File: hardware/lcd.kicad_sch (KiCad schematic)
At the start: 7 parts, among them J3 Conn_01x40, Q3 AO3400A

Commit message: add (analog) mems microphone
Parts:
- R29, R30, R31: footprint (none) -> Resistor_SMD:R_0603_1608Metric
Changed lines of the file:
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@@
 			)
 		)
-		(property "Footprint" ""
+		(property "Footprint" "Resistor_SMD:R_0603_1608Metric"
 			(at 83.82 173.482 90)
 			(effects
@@
 			)
 		)
-		(property "Footprint" ""
+		(property "Footprint" "Resistor_SMD:R_0603_1608Metric"
 			(at 46.99 109.728 90)
 			(effects
@@
 			)
 		)
-		(property "Footprint" ""
+		(property "Footprint" "Resistor_SMD:R_0603_1608Metric"
 			(at 83.82 183.642 90)
 			(effects

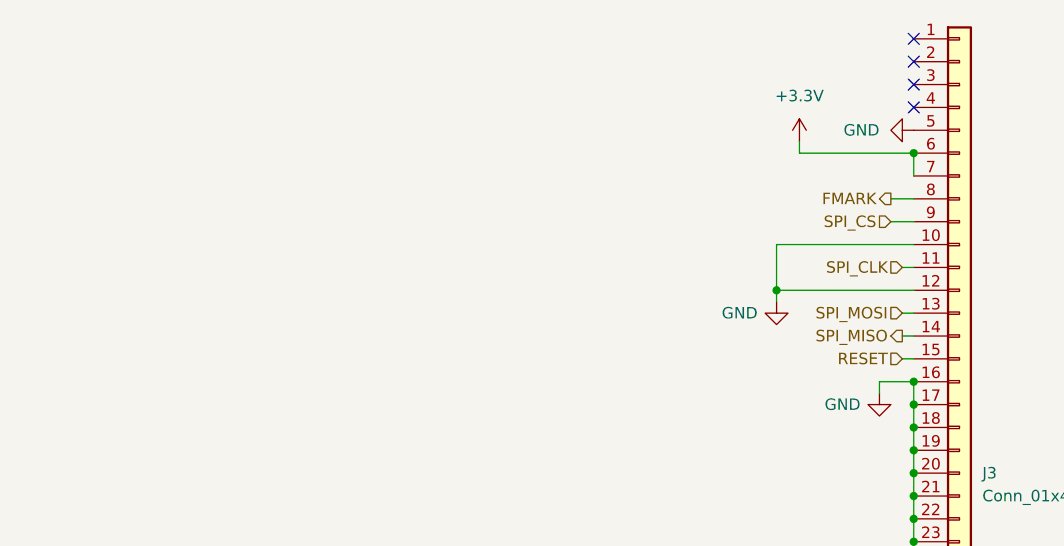
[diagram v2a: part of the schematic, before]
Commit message: Create a preliminary routing
Disconnect the LORA module from the lcd bus
Add netclass and lenght matching rule for the LCD signals
Use Bus for spi syglas for easy netclass association
Remove cutaway jumper for the io expansions, and hardcode the address
Routed the keyboard matrix
Change the LCD resistor to 1202
Fix the0Ohm resistor footprint
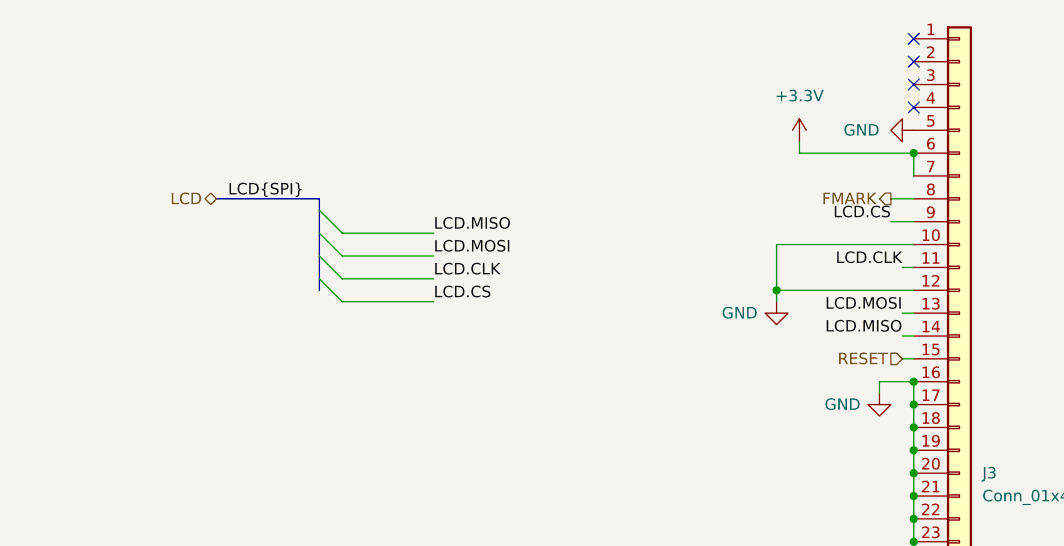
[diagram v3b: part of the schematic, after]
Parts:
- R28: footprint lib:SKRHABE010_ALPS -> Resistor_SMD:R_0603_1608Metric
- R32: footprint (none) -> Resistor_SMD:R_1206_3216Metric
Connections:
- net SPI_CLK renamed LCD.CLK
- net SPI_CS renamed LCD.CS
- net SPI_MISO renamed LCD.MISO
- net SPI_MOSI renamed LCD.MOSI
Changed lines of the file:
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@@
 		(at 133.35 43.18)
 	)
+	(bus_entry
+		(at 67.31 57.15)
+		(size 2.54 2.54)
+		(stroke
+			(width 0)
+			(type default)
+		)
+	)
+	(bus_entry
+		(at 67.31 59.69)
+		(size 2.54 2.54)
+		(stroke
+			(width 0)
+			(type default)
+		)
+	)
+	(bus_entry
+		(at 67.31 64.77)
+		(size 2.54 2.54)
+		(stroke
+			(width 0)
+			(type default)
+		)
+	)
+	(bus_entry
+		(at 67.31 62.23)
+		(size 2.54 2.54)
+		(stroke
+			(width 0)
+			(type default)
+		)
+	)
 	(wire
 		(pts
@@
 		)
 	)
+	(bus
+		(pts
+			(xy 67.31 55.88) (xy 67.31 57.15)
+		)
+		(stroke
+			(width 0)
+			(type default)
+		)
+	)
 	(wire
 		(pts
@@
 		)
 	)
+	(bus
+		(pts
+			(xy 67.31 62.23) (xy 67.31 64.77)
+		)
+		(stroke
+			(width 0)
+			(type default)
+		)
+	)
 	(wire
 		(pts
@@
 		)
 	)
+	(bus
+		(pts
+			(xy 67.31 59.69) (xy 67.31 62.23)
+		)
+		(stroke
+			(width 0)
+			(type default)
+		)
+	)
 	(wire
 		(pts
@@
 	(wire
 		(pts
+			(xy 69.85 64.77) (xy 80.01 64.77)
+		)
+		(stroke
+			(width 0)
+			(type default)
+		)
+	)
+	(wire
+		(pts
 			(xy 59.69 115.57) (xy 63.5 115.57)
 		)
@@
 	(wire
 		(pts
+			(xy 69.85 67.31) (xy 80.01 67.31)
+		)
+		(stroke
+			(width 0)
+			(type default)
+		)
+	)
+	(wire
+		(pts
 			(xy 74.93 185.42) (xy 80.01 185.42)
 		)
@@
 		)
 	)
+	(bus
+		(pts
+			(xy 67.31 64.77) (xy 67.31 66.04)
+		)
+		(stroke
+			(width 0)
+			(type default)
+		)
+	)
 	(wire
 		(pts
@@
 		)
 	)
+	(bus
+		(pts
+			(xy 67.31 57.15) (xy 67.31 59.69)
+		)
+		(stroke
+			(width 0)
+			(type default)
+		)
+	)
 	(wire
 		(pts
@@
 		)
 	)
+	(bus
+		(pts
+			(xy 55.88 55.88) (xy 67.31 55.88)
+		)
+		(stroke
+			(width 0)
+			(type default)
+		)
+	)
 	(wire
 		(pts
@@
 	(wire
 		(pts
+			(xy 69.85 59.69) (xy 80.01 59.69)
+		)
+		(stroke
+			(width 0)
+			(type default)
+		)
+	)
+	(wire
+		(pts
 			(xy 128.27 132.08) (xy 133.35 132.08)
 		)
@@
 	(wire
 		(pts
+			(xy 69.85 62.23) (xy 80.01 62.23)
+		)
+		(stroke
+			(width 0)
+			(type default)
+		)
+	)
+	(wire
+		(pts
 			(xy 132.08 71.12) (xy 133.35 71.12)
 		)
@@
 		)
 	)
+	(label "LCD.MISO"
+		(at 80.01 59.69 0)
+		(effects
+			(font
+				(size 1.27 1.27)
+			)
+			(justify left bottom)
+		)
+		(property "Netclass" "LCD"
+			(at 80.01 59.69 0)
+			(effects
+				(font
+					(size 1.27 1.27)
+					(italic yes)
+				)
+				(hide yes)
+			)
+		)
+	)
 	(label "IM1"
 		(at 128.27 134.62 0)
@@
 		)
 	)
+	(label "LCD.MISO"
+		(at 132.08 71.12 180)
+		(fields_autoplaced yes)
+		(effects
+			(font
+				(size 1.27 1.27)
+			)
+			(justify right bottom)
+		)
+	)
 	(label "IM0"
 		(at 128.27 132.08 0)
@@
 		)
 	)
+	(label "LCD.MOSI"
+		(at 80.01 62.23 0)
+		(effects
+			(font
+				(size 1.27 1.27)
+			)
+			(justify left bottom)
+		)
+	)
 	(label "LEDK"
 		(at 77.47 115.57 180)
@@
 		)
 	)
+	(label "LCD.CS"
+		(at 80.01 67.31 0)
+		(effects
+			(font
+				(size 1.27 1.27)
+			)
+			(justify left bottom)
+		)
+	)
+	(label "LCD{SPI}"
+		(at 57.15 55.88 0)
+		(effects
+			(font
+				(size 1.27 1.27)
+			)
+			(justify left bottom)
+		)
+	)
 	(label "IM0"
 		(at 74.93 165.1 0)
@@
 		)
 	)
-	(label "IM1"
-		(at 74.93 175.26 0)
+	(label "LCD.CS"
+		(at 130.81 58.42 180)
 		(fields_autoplaced yes)
 		(effects
@@
 				(size 1.27 1.27)
 			)
-			(justify left bottom)
+			(justify right bottom)
 		)
 	)
-	(hierarchical_label "SPI_CS"
-		(shape input)
-		(at 130.81 58.42 180)
+	(label "LCD.MOSI"
+		(at 132.08 68.58 180)
 		(fields_autoplaced yes)
 		(effects
@@
 				(size 1.27 1.27)
 			)
-			(justify right)
+			(justify right bottom)
 		)
 	)
-	(hierarchical_label "SPI_MISO"
-		(shape output)
-		(at 132.08 71.12 180)
+	(label "IM1"
+		(at 74.93 175.26 0)
 		(fields_autoplaced yes)
 		(effects
@@
 				(size 1.27 1.27)
 			)
-			(justify right)
+			(justify left bottom)
 		)
 	)
-	(hierarchical_label "SPI_CLK"
-		(shape input)
+	(label "LCD.CLK"
 		(at 132.08 63.5 180)
 		(fields_autoplaced yes)
@@
 				(size 1.27 1.27)
 			)
-			(justify right)
+			(justify right bottom)
 		)
 	)
-	(hierarchical_label "BACKLIGHT"
-		(shape input)
-		(at 40.64 107.95 180)
+	(label "LCD.CLK"
+		(at 80.01 64.77 0)
+		(effects
+			(font
+				(size 1.27 1.27)
+			)
+			(justify left bottom)
+		)
+	)
+	(hierarchical_label "LCD"
+		(shape bidirectional)
+		(at 55.88 55.88 180)
 		(fields_autoplaced yes)
 		(effects
@@
 		)
 	)
-	(hierarchical_label "RESET"
+	(hierarchical_label "BACKLIGHT"
 		(shape input)
-		(at 132.08 73.66 180)
+		(at 40.64 107.95 180)
 		(fields_autoplaced yes)
 		(effects
@@
 		)
 	)
-	(hierarchical_label "SPI_MOSI"
+	(hierarchical_label "RESET"
 		(shape input)
-		(at 132.08 68.58 180)
+		(at 132.08 73.66 180)
 		(fields_autoplaced yes)
 		(effects
@@
 			)
 		)
-		(property "Footprint" ""
+		(property "Footprint" "Resistor_SMD:R_1206_3216Metric"
 			(at 67.31 117.348 90)
 			(effects
@@
 			)
 		)
-		(property "Footprint" "lib:SKRHABE010_ALPS"
+		(property "Footprint" "Resistor_SMD:R_0603_1608Metric"
 			(at 83.82 166.878 90)
 			(effects

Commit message: Move usb to the opposite side of the PCB
Change the lcd SPI pins and use ones dirrectly atatched to SPI2
Lengh tune the LCD spi line and USB
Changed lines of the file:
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@@
 		)
 	)
+	(bus
+		(pts
+			(xy 67.31 64.77) (xy 67.31 67.31)
+		)
+		(stroke
+			(width 0)
+			(type default)
+		)
+	)
 	(wire
 		(pts
@@
 		)
 	)
-	(bus
-		(pts
-			(xy 67.31 64.77) (xy 67.31 66.04)
-		)
-		(stroke
-			(width 0)
-			(type default)
-		)
-	)
 	(wire
 		(pts
@@
 	)
 	(label "LCD.MISO"
-		(at 80.01 59.69 0)
+		(at 80.01 59.69 180)
 		(effects
 			(font
 				(size 1.27 1.27)
 			)
-			(justify left bottom)
+			(justify right bottom)
 		)
 		(property "Netclass" "LCD"
@@
 	)
 	(label "LCD.MOSI"
-		(at 80.01 62.23 0)
+		(at 80.01 62.23 180)
+		(fields_autoplaced yes)
 		(effects
 			(font
 				(size 1.27 1.27)
 			)
-			(justify left bottom)
+			(justify right bottom)
 		)
 	)
@@
 	)
 	(label "LCD.CS"
-		(at 80.01 67.31 0)
+		(at 80.01 67.31 180)
+		(fields_autoplaced yes)
 		(effects
 			(font
 				(size 1.27 1.27)
 			)
-			(justify left bottom)
+			(justify right bottom)
 		)
 	)
 	(label "LCD{SPI}"
 		(at 57.15 55.88 0)
+		(fields_autoplaced yes)
 		(effects
 			(font
@@
 	)
 	(label "LCD.CLK"
-		(at 80.01 64.77 0)
+		(at 80.01 64.77 180)
+		(fields_autoplaced yes)
 		(effects
 			(font
 				(size 1.27 1.27)
 			)
-			(justify left bottom)
+			(justify right bottom)
 		)
 	)

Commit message: Route all board
Fix CS missing for SD card
Add IMU symbol and footprint to the project lib
Finish esp32 pinswaps
Move non critical signals to the keyboard IO expander
Add power flag symbols
Fix Dpad pin type
Fix IMU pin type
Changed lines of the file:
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@@
 		)
 	)
-	(hierarchical_label "LCD"
+	(hierarchical_label "LCD{SPI}"
 		(shape bidirectional)
 		(at 55.88 55.88 180)

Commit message: Associate all LCSC component
Change sdcard pullup resistor to 47K
Center main schematic
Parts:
- J3: LCSC (none) -> C202114
- R28, R29, R30: LCSC (none) -> C116699
- R31: LCSC (none) -> C105588
- R32: LCSC (none) -> C308517
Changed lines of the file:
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@@
+			)
+		)
+		(property "LCSC" "C116699"
+			(at 83.82 175.26 0)
+			(effects
+				(font
+					(size 1.27 1.27)
+				)
+				(hide yes)
 			)
 		)
@@
 			)
 		)
+		(property "LCSC" "C308517"
+			(at 67.31 115.57 0)
+			(effects
+				(font
+					(size 1.27 1.27)
+				)
+				(hide yes)
+			)
+		)
 		(pin "2"
 		)
@@
 			)
 		)
+		(property "LCSC" "C116699"
+			(at 83.82 165.1 0)
+			(effects
+				(font
+					(size 1.27 1.27)
+				)
+				(hide yes)
+			)
+		)
 		(pin "2"
 		)
@@
 			)
 		)
+		(property "LCSC" "C105588"
+			(at 46.99 107.95 0)
+			(effects
+				(font
+					(size 1.27 1.27)
+				)
+				(hide yes)
+			)
+		)
 		(pin "2"
 		)
@@
 			)
 		)
+		(property "LCSC" "C116699"
+			(at 83.82 185.42 0)
+			(effects
+				(font
+					(size 1.27 1.27)
+				)
+				(hide yes)
+			)
+		)
 		(pin "2"
 		)
@@
 			(at 138.43 86.36 0)
 			(effects
+				(font
+					(size 1.27 1.27)
+				)
+				(hide yes)
+			)
+		)
+		(property "LCSC" "C202114"
+			(at 138.43 86.36 0)
+			(effects

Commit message: update bom, correct jlcpcb rotation
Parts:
- J3: JLCPCB Rotation Offset (none) -> 180
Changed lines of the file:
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@@
+			)
+		)
+		(property "JLCPCB Rotation Offset" "180"
+			(at 138.43 86.36 0)
+			(effects
+				(font
+					(size 1.27 1.27)
+				)
+				(hide yes)
 			)
 		)
